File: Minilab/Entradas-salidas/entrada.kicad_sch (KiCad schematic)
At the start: 52 parts, among them J0 In 5V, J1 Out 5V/0V, J10 Vin, J11 Vin, J12 Vin, J13 In 5V, J14 In 5V, J2 Out 5V/0V, J3 Out 5V/0V, J4 Out 5V/0V, J5 Out 5V/0V, J6 Out 5V/0V, J7 Vin, J8 Vin, J9 Vin, SW1 SW_SPST, SW2 SW_SPST, SW3 SW_SPST, SW4 SW_SPST, SW5 SW_SPST, SW6 SW_SPST, SW8 SW_DIP_x07

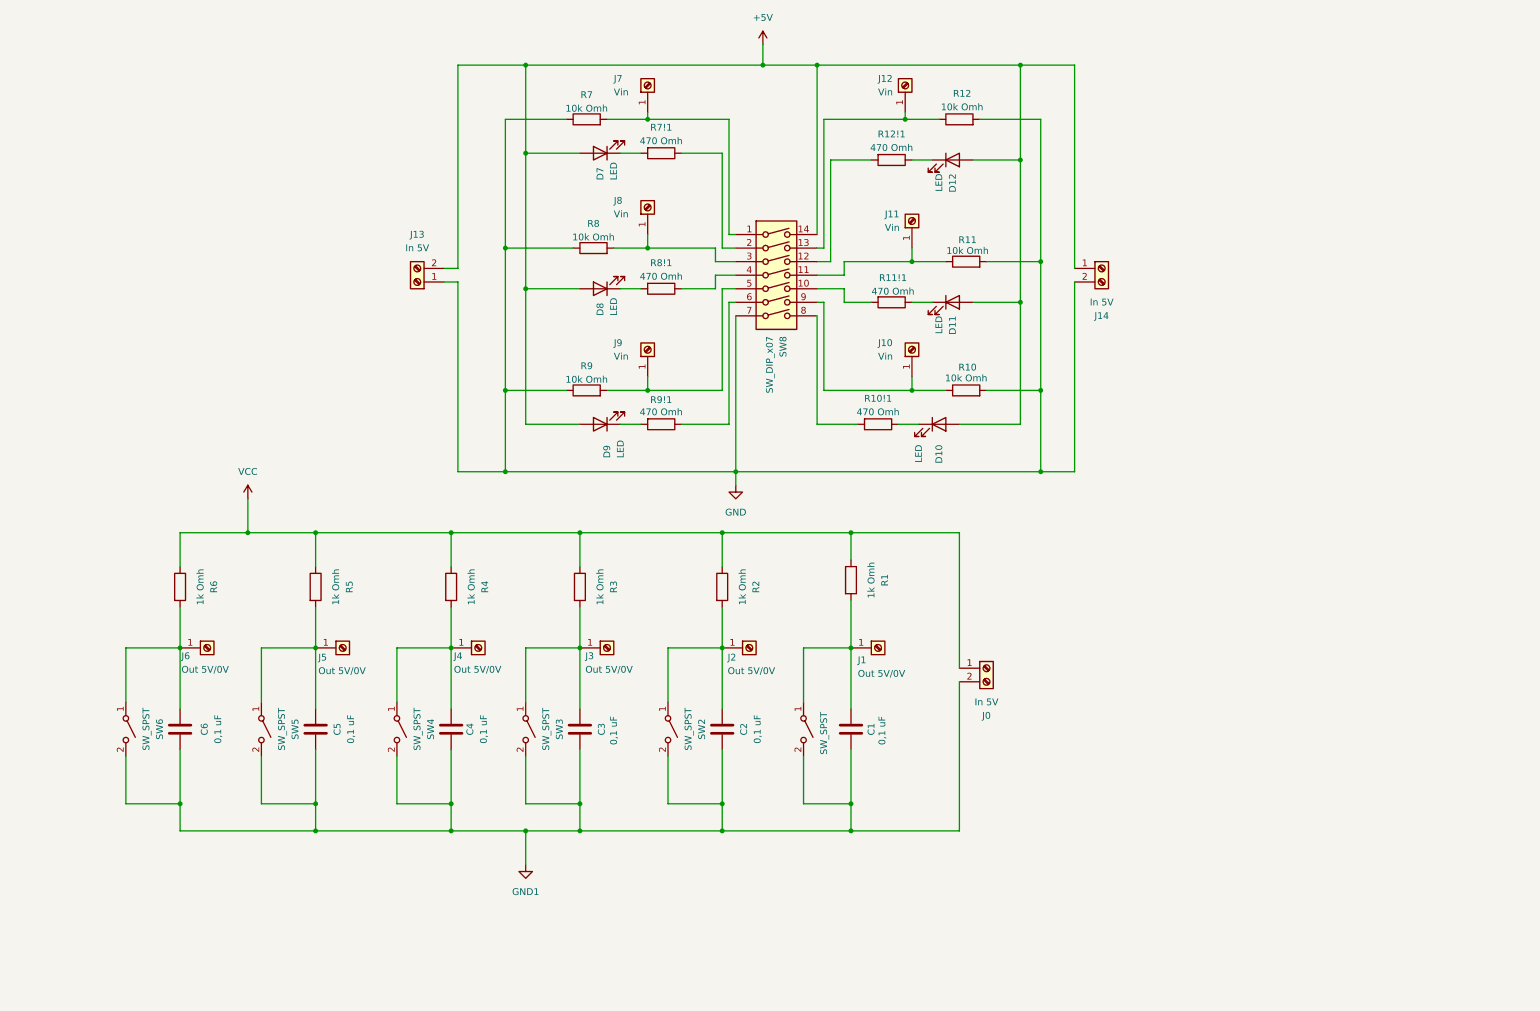
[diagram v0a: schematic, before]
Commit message: cambio de CI de entradas y oscilador
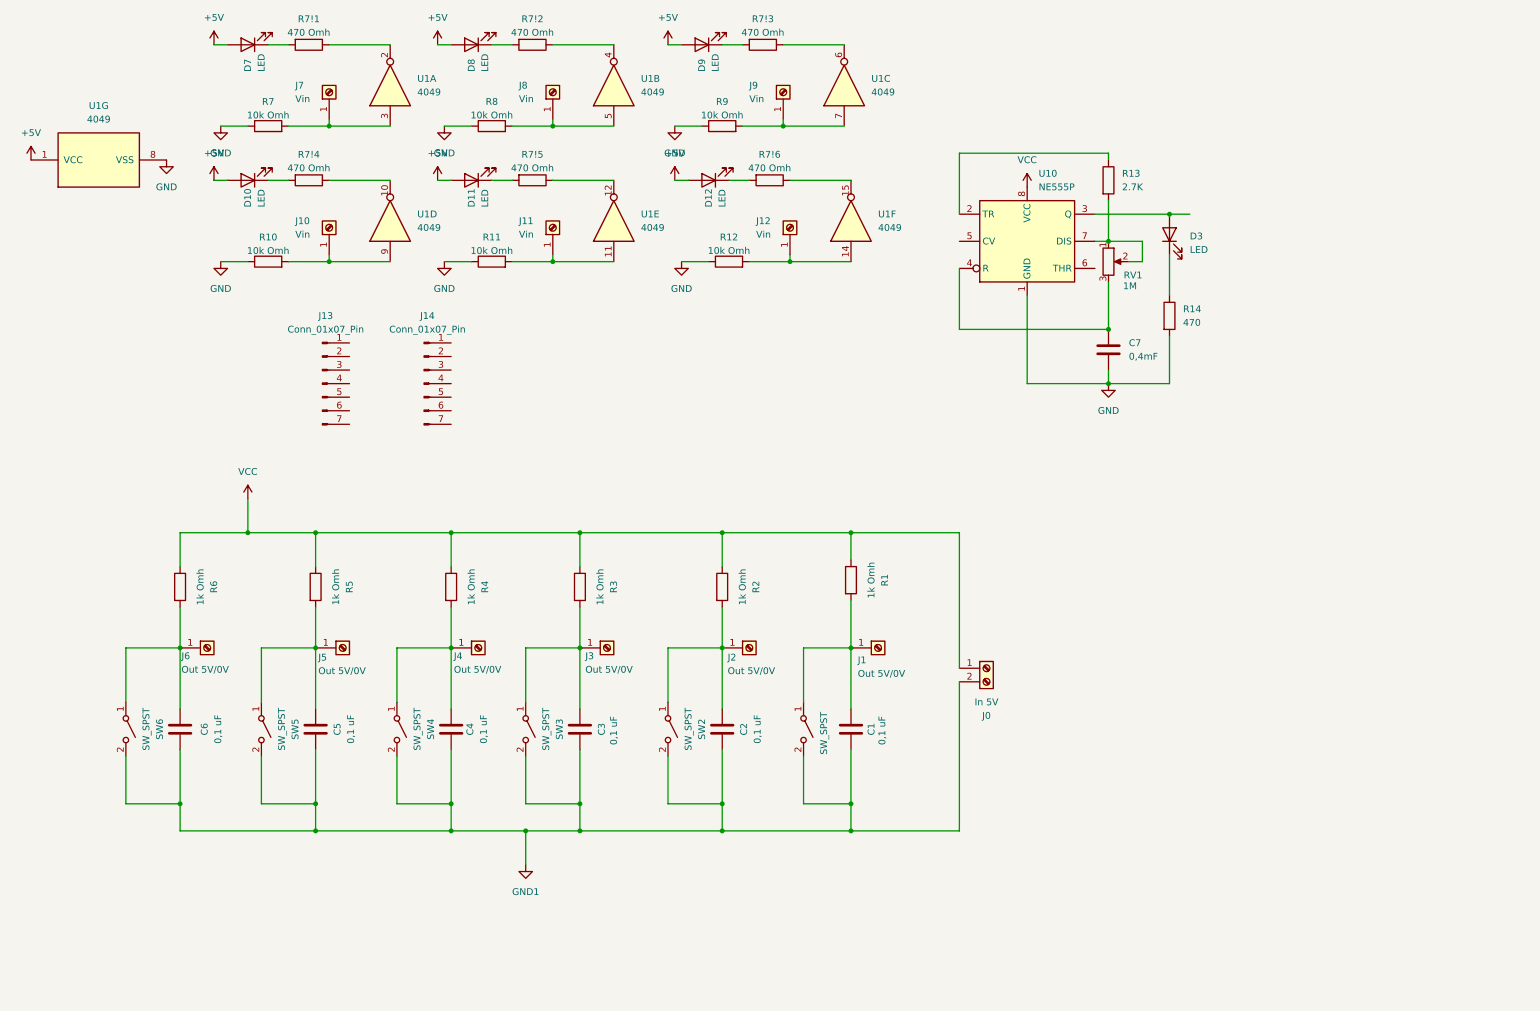
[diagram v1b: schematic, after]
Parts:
- removed J13, J14: In 5V, Connector_Molex:Molex_KK-254_AE-6410-02A_1x02_P2.54mm_Vertical, symbol Connector:Screw_Terminal_01x02
- removed R10!1, R11!1, R12!1, R8!1, R9!1: 470 Omh, Resistor_THT:R_Axial_DIN0204_L3.6mm_D1.6mm_P7.62mm_Horizontal, symbol Device:R
- removed SW8: SW_DIP_x07, Package_DIP:DIP-14_W7.62mm_Socket, symbol Switch:SW_DIP_x07
- added C7: 0,4mF, symbol Device:C
- added D3: LED, symbol Device:LED
- added J13, J14: Conn_01x07_Pin, symbol Connector:Conn_01x07_Pin
- added R13: 2.7K, symbol Device:R
- added R14: 470, symbol Device:R
- added R7!2, R7!3, R7!4, R7!5, R7!6: 470 Omh, Resistor_THT:R_Axial_DIN0204_L3.6mm_D1.6mm_P7.62mm_Horizontal, symbol Device:R
- added RV1: 1M, symbol Device:R_Potentiometer
- added U1: 4049, Package_DIP:CERDIP-16_W7.62mm_SideBrazed, symbol 4xxx:4049
- added U10: NE555P, Package_DIP:DIP-8_W7.62mm, symbol Timer:NE555P
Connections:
- net +5V: now also U1.1 (VCC)
- net GND: now also R10.1, R11.1, R12.1, C7.2, R14.2, U1.8 (VSS), U10.1 (GND); no longer R10.2, R11.2, R12.2
- net VCC: now also U10.8 (VCC)
- net at J12.1 (Pin_1): now also R12.2, U1.14; no longer R12.1
- net at D10.1 (K): now also R7!4.2
- net at D8.1 (K): now also R7!2.2
- net at J9.1 (Pin_1), R9.2: now also U1.7
- net at D11.1 (K): now also R7!5.2
- net at J8.1 (Pin_1), R8.2: now also U1.5
- net at J7.1 (Pin_1), R7.2: now also U1.3
- net at J10.1 (Pin_1): now also R10.2, U1.9; no longer R10.1
- net at J11.1 (Pin_1): now also R11.2, U1.11; no longer R11.1
- net at D12.1 (K): now also R7!6.2
- net at R7!1.1: now also U1.2
- net at D9.1 (K): now also R7!3.2
- new net: R7!2.1, U1.4
- new net: R7!3.1, U1.6
- new net: R7!5.1, U1.12
- new net: D3.1 (K), R14.1
- new net: D3.2 (A), U10.3 (Q)
- new net: R13.2, RV1.1, RV1.2, U10.7 (DIS)
- new net: C7.1, RV1.3, U10.4 (R)
- new net: R13.1, U10.2 (TR)
- new net: R7!4.1, U1.10
- new net: R7!6.1, U1.15
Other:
- moved on the sheet: D7, J7, R7, R7!1

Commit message: Continuacion .sch
Continuacion .sch
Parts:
- removed D10, D11, D7, D8, D9: LED, LED_THT:LED_D5.0mm, symbol Device:LED
- removed J0: In 5V, Connector_Molex:Molex_KK-254_AE-6410-02A_1x02_P2.54mm_Vertical, symbol Connector:Screw_Terminal_01x02
- removed J10, J11, J7, J8, J9: Vin, Connector_PinHeader_1.00mm:PinHeader_1x01_P1.00mm_Vertical, symbol Connector:Screw_Terminal_01x01
- added D13, D14, D15, D16, D17: LED, LED_THT:LED_D5.0mm, symbol Device:LED
- added J15, J23: Conn_01x07_Pin, symbol Connector:Conn_01x07_Pin
- added J16, J22: Conn_01x06_Pin, symbol Connector:Conn_01x06_Pin
- added J17, J18, J19, J20, J21: Vin, Connector_PinHeader_1.00mm:PinHeader_1x01_P1.00mm_Vertical, symbol Connector:Screw_Terminal_01x01
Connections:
- net +5V: no longer D12.2 (A)
- net GND: now also J16.1 (Pin_1)
- net GND1: now also J14.7 (Pin_7)
- net PinBOut: now reaches R7!2.2
- net PinBOut: now also J15.5 (Pin_5)
- net PinCOut: now reaches R7!3.2
- net PinCOut: now also J15.4 (Pin_4)
- net PinDOut: now reaches R7!4.2
- net PinDOut: now also J15.3 (Pin_3)
- net PinEOut: now reaches R7!5.2
- net PinEOut: now also J15.2 (Pin_2)
- net PinC5: now reaches C5.2, J5.1 (Pin_1), SW5.1 (A)
- net PinC5: now also J14.5 (Pin_5); no longer R5.2
- net PinC3: now reaches C3.2, J3.1 (Pin_1), SW3.1 (A)
- net PinC3: now also J14.3 (Pin_3); no longer R3.2
- net PinC1: now reaches C1.2, J1.1 (Pin_1), SW1.1 (A)
- net PinC1: now also J14.1 (Pin_1); no longer R1.2
- net PinDIn: now reaches R10.2, U1.9
- net PinDIn: now also J16.3 (Pin_3)
- net PinAIn: now reaches R7.2, U1.3
- net PinAIn: now also J16.6 (Pin_6)
- net PinCIn: now reaches R9.2, U1.7
- net PinCIn: now also J16.4 (Pin_4)
- net PinR6: now reaches J13.1 (Pin_1)
- net PinR6: now also R6.2
- net PinR5: now reaches J13.2 (Pin_2)
- net PinR5: now also R5.2
- net PinR4: now reaches J13.3 (Pin_3)
- net PinR4: now also R4.2
- net PinR3: now reaches J13.4 (Pin_4)
- net PinR3: now also R3.2
- net PinR2: now reaches J13.5 (Pin_5)
- net PinR2: now also R2.2
- net PinR1: now reaches J13.6 (Pin_6)
- net PinR1: now also R1.2
- net PinGND: now reaches J13.7 (Pin_7)
- net at R12.2, U1.14: no longer J12.1 (Pin_1)
- net PinBIn: now reaches R8.2, U1.5
- net PinBIn: now also J16.5 (Pin_5)
- net PinAOut: now reaches R7!1.2
- net PinAOut: now also J15.6 (Pin_6)
- net PinEIn: now reaches R11.2, U1.11
- net PinEIn: now also J16.2 (Pin_2)
- net PinC4: now reaches C4.2, J4.1 (Pin_1), SW4.1 (A)
- net PinC4: now also J14.4 (Pin_4); no longer R4.2
- net PinFOut: now reaches R7!6.2
- net PinFOut: now also J15.1 (Pin_1); no longer D12.1 (K)
- net PinC2: now reaches C2.2, J2.1 (Pin_1), SW2.1 (A)
- net PinC2: now also J14.2 (Pin_2); no longer R2.2
- net PinC6: now reaches C6.2, J6.1 (Pin_1), SW6.1 (A)
- net PinC6: now also J14.6 (Pin_6); no longer R6.2
- new net PinAIn1: J17.1 (Pin_1), J22.6 (Pin_6)
- new net PinAOut1: D13.1 (K), J23.6 (Pin_6)
- new net PinBIn1: J12.1 (Pin_1), J22.5 (Pin_5)
- new net PinBOut1: D16.1 (K), J23.5 (Pin_5)
- new net PinCIn1: J18.1 (Pin_1), J22.4 (Pin_4)
- new net PinCOut1: D14.1 (K), J23.4 (Pin_4)
- new net PinDIn1: J19.1 (Pin_1), J22.3 (Pin_3)
- new net PinDOut1: D15.1 (K), J23.3 (Pin_3)
- new net PinEIn1: J21.1 (Pin_1), J22.2 (Pin_2)
- new net PinEOut1: D17.1 (K), J23.2 (Pin_2)
- new net PinFIn1: J20.1 (Pin_1), J22.1 (Pin_1)
- new net PinFOut1: D12.1 (K), J23.1 (Pin_1)
- new net PinVCCLed: J15.7 (Pin_7)
- new net PinVCCLed1: D12.2 (A), D13.2 (A), D14.2 (A), D15.2 (A), D16.2 (A), D17.2 (A), J23.7 (Pin_7)
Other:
- moved on the sheet: C7, D12, D3, J12, J13, R1, R12, R13, R14, R2, R3, R4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

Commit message: Ordeno un poco
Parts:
- J13: value Conn_01x07_Pin -> Conn_01x07_Pin_PlacaPrincipal
- J14: value Conn_01x07_Pin -> Conn_01x07_Pin_PlacaSecu
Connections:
- net GND: no longer J16.1 (Pin_1)
- net PinFIn: now reaches R12.2, U1.14
- net PinFIn: now also J16.1 (Pin_1)
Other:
- moved on the sheet: C1, C2, C3, C4, C5, C6, C7, D12, D13, D14, D15, D16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

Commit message: casi terminado .sch
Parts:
- removed J13: Conn_01x07_Pin_PlacaPrincipal, symbol Connector:Conn_01x07_Pin
- removed J14: Conn_01x07_Pin_PlacaSecu, symbol Connector:Conn_01x07_Pin
- added J10: Conn_01x10_Pin, Connector_PinHeader_2.54mm:PinHeader_1x10_P2.54mm_Vertical, symbol Connector:Conn_01x10_Pin
- added J24, J25, J26: Vin, Connector_PinSocket_2.00mm:PinSocket_1x01_P2.00mm_Vertical, symbol Connector:Screw_Terminal_01x01
- added J7: USB_B_Micro, Connector_USB:USB3_A_Molex_48393-001, symbol Connector:USB_B_Micro
- added J8: Jack-DC, Connector_BarrelJack:BarrelJack_Horizontal, symbol Connector:Jack-DC
- added J9: Conn_01x10_Pin, Connector_PinSocket_2.54mm:PinSocket_1x10_P2.54mm_Vertical, symbol Connector:Conn_01x10_Pin
- D3: footprint (none) -> LED_THT:LED_D5.0mm
- J1, J17, J18, J19, J2, J20, J21, J3, J4, J5, J6: footprint Connector_PinHeader_1.00mm:PinHeader_1x01_P1.00mm_Vertical -> Connector_PinSocket_2.00mm:PinSocket_1x01_P2.00mm_Vertical
- J15: footprint (none) -> Connector_PinHeader_2.54mm:PinHeader_1x07_P2.54mm_Vertical
- J16: footprint (none) -> Connector_PinHeader_2.54mm:PinHeader_1x06_P2.54mm_Vertical
- J22: footprint (none) -> Connector_PinSocket_2.54mm:PinSocket_1x06_P2.54mm_Vertical
- J23: footprint (none) -> Connector_PinSocket_2.54mm:PinSocket_1x07_P2.54mm_Vertical
- R13, R14: footprint (none) -> Resistor_THT:R_Axial_DIN0204_L3.6mm_D1.6mm_P7.62mm_Horizontal
- RV1: value 1M -> 5K; footprint (none) -> Potentiometer_THT:Potentiometer_Omeg_PC16BU_Horizontal
- U1: footprint (none) -> Package_DIP:CERDIP-16_W7.62mm_SideBrazed
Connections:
- net +5V is gone; now on net VCC: U1.1 (VCC)
- net GND1 is gone; now on net GNDSw: C1.1, C2.1, C3.1, C4.1, C5.1, C6.1, SW1.2 (B), SW2.2 (B), SW3.2 (B), SW4.2 (B), SW5.2 (B), SW6.2 (B)
- net PinVCCLed is gone; now on net VCC: J15.7 (Pin_7)
- net GND: now also J10.10 (Pin_10), J7.5 (GND), J8.2; no longer R14.2
- net PinC1: now also J9.1 (Pin_1)
- net PinC2: now also J9.2 (Pin_2)
- net PinC3: now also J9.3 (Pin_3)
- net PinC4: now also J9.4 (Pin_4)
- net PinC5: now also J9.5 (Pin_5)
- net PinC6: now also J9.6 (Pin_6)
- net PinR1: now also J10.6 (Pin_6)
- net PinR2: now also J10.5 (Pin_5)
- net PinR3: now also J10.4 (Pin_4)
- net PinR4: now also J10.3 (Pin_3)
- net PinR5: now also J10.2 (Pin_2)
- net PinR6: now also J10.1 (Pin_1)
- net VCC: now also J10.9 (Pin_9), J7.1 (VBUS), J8.1
- net GNDSw: now reaches D3.1 (K)
- net GNDSw: now also RV1.3, J25.1 (Pin_1), J9.10 (Pin_10); no longer R14.1
- net at D3.2 (A): now also R14.2; no longer U10.3 (Q)
- net PinPot1: now reaches R13.2, U10.7 (DIS)
- net PinPot1: no longer RV1.1, RV1.2
- net PinPot3: now reaches C7.1, U10.4 (R)
- net PinPot3: no longer RV1.3
- net PinVCCLed1 renamed VCCLed
- net VCCLed: now also J26.1 (Pin_1)
- new net OscOut: J10.7 (Pin_7), U10.3 (Q)
- new net OscOut1: J24.1 (Pin_1), J9.7 (Pin_7), R14.1
- new net PinPotOut: J10.8 (Pin_8)
- new net PinPotOut1: J9.8 (Pin_8), RV1.2
- new net VCCSw: J9.9 (Pin_9), RV1.1
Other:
- moved on the sheet: C1, C2, C3, C4, C5, C6, C7, D3, J1, J2, J3, J4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

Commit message: avance pcb y agregado mini360
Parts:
- added U2: Mini360, Mini360:Mini360_step-down, symbol Mini 360:Mini360
- J12: footprint Connector_PinHeader_1.00mm:PinHeader_1x01_P1.00mm_Vertical -> Connector_PinSocket_2.00mm:PinSocket_1x01_P2.00mm_Vertical
- J_USB1: renamed from J7; footprint Connector_USB:USB3_A_Molex_48393-001 -> Connector_USB:USB_Micro-B_Molex_47346-0001
- SW1, SW2, SW3, SW4, SW5, SW6: footprint Button_Switch_THT:SW_CuK_OS102011MA1QN1_SPDT_Angled -> Button_Switch_THT:SW_Slide_SPDT_Straight_CK_OS102011MS2Q
- renumbered D3 to D1, D13 to D2, D16 to D3, D14 to D4, D15 to D5, D17 to D6, D12 to D7, J19 to J10, J18 to J11, J17 to J13, J9 to J14, J25 to J15, J24 to J16, J26 to J7, J20 to J8, J21 to J9, J10 to JP1, J15 to JP2, J16 to JP3, J22 to JP4, J23 to JP5, J8 to J_JACK1, R7!4 to R10!1, R7!5 to R11!1, R7!6 to R12!1, R7!2 to R8!1, R7!3 to R9!1
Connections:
- net GND: now also U2.1 (IN-)
- net VCC: now also U2.4 (OUT+); no longer J_JACK1.1, J_USB1.1 (VBUS)
- new net VCC_nreg: J_JACK1.1, J_USB1.1 (VBUS), U2.2 (IN+)
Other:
- moved on the sheet: J_JACK1

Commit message: FIN PLACA 2
FIN PLACA 2
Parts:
- removed J14: Conn_01x10_Pin, Connector_PinSocket_2.54mm:PinSocket_1x10_P2.54mm_Vertical, symbol Connector:Conn_01x10_Pin
- removed JP1: Conn_01x10_Pin, Connector_PinHeader_2.54mm:PinHeader_1x10_P2.54mm_Vertical, symbol Connector:Conn_01x10_Pin
- added J17: VCC, Connector_PinSocket_2.00mm:PinSocket_1x01_P2.00mm_Vertical, symbol Connector:Screw_Terminal_01x01
- added J18: OUT, Connector_PinSocket_2.00mm:PinSocket_1x01_P2.00mm_Vertical, symbol Connector:Screw_Terminal_01x01
- added J19: GND, Connector_PinSocket_2.00mm:PinSocket_1x01_P2.00mm_Vertical, symbol Connector:Screw_Terminal_01x01
- added J20: Conn_01x08_Pin, Connector_PinHeader_2.54mm:PinHeader_1x08_P2.54mm_Vertical, symbol Connector:Conn_01x08_Pin
- added J21: Conn_01x08_Pin, Connector_PinSocket_2.54mm:PinSocket_1x08_P2.54mm_Vertical, symbol Connector:Conn_01x08_Pin
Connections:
- net GND: now also J20.8 (Pin_8)
- net GNDSw: now also J21.8 (Pin_8); no longer RV1.3
- net OscOut: now also J20.7 (Pin_7)
- net OscOut1: now also J21.7 (Pin_7)
- net PinC1: now also J21.1 (Pin_1)
- net PinC2: now also J21.2 (Pin_2)
- net PinC3: now also J21.3 (Pin_3)
- net PinC4: now also J21.4 (Pin_4)
- net PinC5: now also J21.5 (Pin_5)
- net PinC6: now also J21.6 (Pin_6)
- net PinPot1: now also J17.1 (Pin_1), J18.1 (Pin_1)
- net PinPot3: now also J19.1 (Pin_1)
- net PinR1: now also J20.6 (Pin_6)
- net PinR2: now also J20.5 (Pin_5)
- net PinR3: now also J20.4 (Pin_4)
- net PinR4: now also J20.3 (Pin_3)
- net PinR5: now also J20.2 (Pin_2)
- net PinR6: now also J20.1 (Pin_1)
- net PinPotOut1: no longer names the net of RV1.2
- net VCCSw: no longer names the net of RV1.1
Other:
- moved on the sheet: D1, J15, J16, R14, RV1

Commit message: revision final
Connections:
- net VCC: now also J_USB1.1 (VBUS)
- net VCC_nreg: no longer J_USB1.1 (VBUS)
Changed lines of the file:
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@@
 			)
 		)
-		(property "Value" "VCC_nreg"
+		(property "Value" "VCC"
 			(at 192.786 92.71 90)
 			(effects

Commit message: hecho plano de masa y tornillos
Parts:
- removed RV1: 5K, Potentiometer_THT:Potentiometer_Omeg_PC16BU_Horizontal, symbol Device:R_Potentiometer
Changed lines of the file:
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@@
-	)
-	(symbol
-		(lib_id "Device:R_Potentiometer")
-		(at 208.28 120.65 0)
-		(unit 1)
-		(exclude_from_sim no)
-		(in_bom yes)
-		(on_board yes)
-		(dnp no)
-		(fields_autoplaced yes)
-		(property "Reference" "RV1"
-			(at 205.74 119.3799 0)
-			(effects
-				(font
-					(size 1.27 1.27)
-				)
-				(justify right)
-			)
-		)
-		(property "Value" "5K"
-			(at 205.74 121.9199 0)
-			(effects
-				(font
-					(size 1.27 1.27)
-				)
-				(justify right)
-			)
-		)
-		(property "Footprint" "Potentiometer_THT:Potentiometer_Omeg_PC16BU_Horizontal"
-			(at 208.28 120.65 0)
-			(effects
-				(font
-					(size 1.27 1.27)
-				)
-				(hide yes)
-			)
-		)
-		(property "Datasheet" "~"
-			(at 208.28 120.65 0)
-			(effects
-				(font
-					(size 1.27 1.27)
-				)
-				(hide yes)
-			)
-		)
-		(property "Description" "Potentiometer"
-			(at 208.28 120.65 0)
-			(effects
-				(font
-					(size 1.27 1.27)
-				)
-				(hide yes)
-			)
-		)
-		(pin "2"
-		)
-		(pin "1"
-		)
-		(pin "3"
-		)
-		(instances
-			(project ""
-				(path "/d0c6dfcb-2af4-4ca4-8d47-0c5bb3467b73"
-					(reference "RV1")
-					(unit 1)
-				)
-			)
-		)
 	)
 	(symbol
